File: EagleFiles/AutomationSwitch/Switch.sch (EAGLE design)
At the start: 28 parts, among them IC1 5V, U1 ATMEGA328P_PDIP

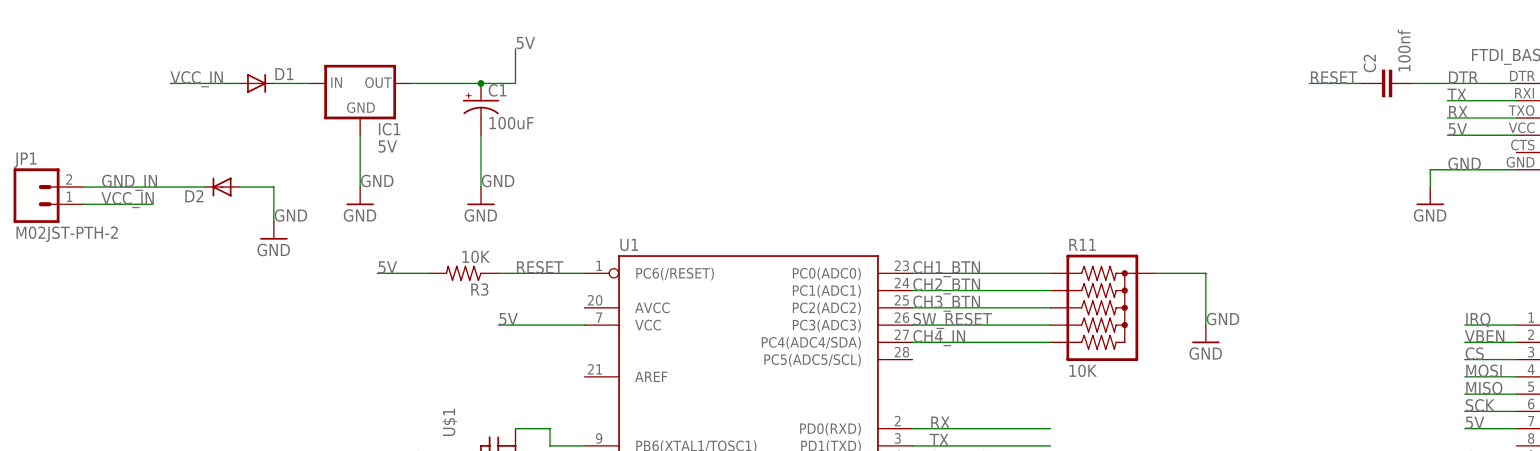
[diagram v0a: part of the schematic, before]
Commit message: Reworked routing and power
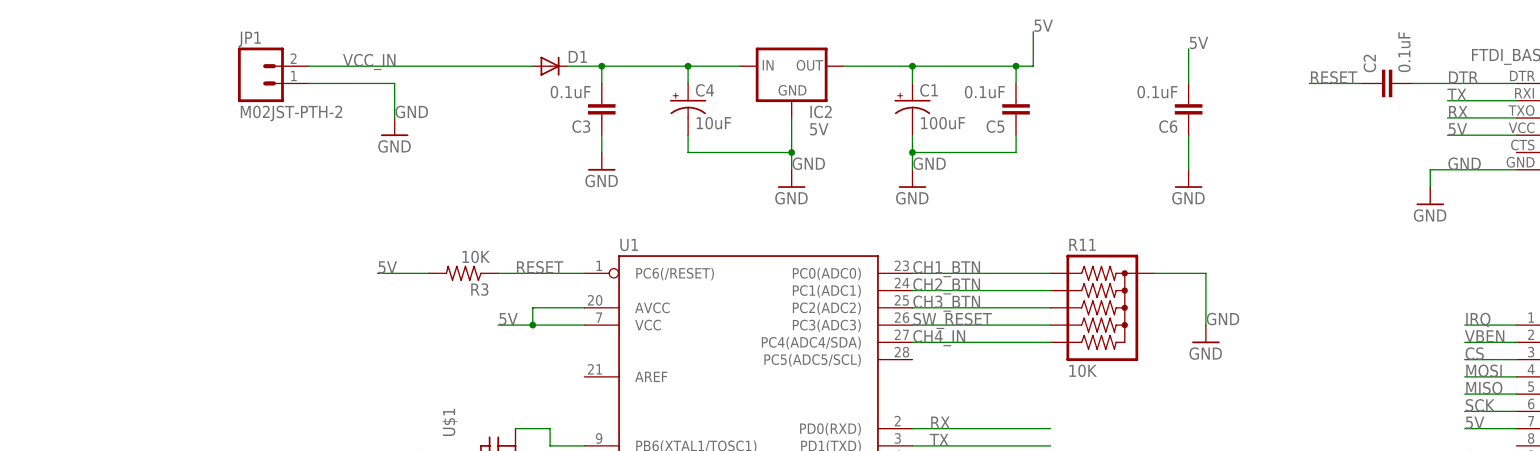
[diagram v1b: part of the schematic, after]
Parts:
- removed D2: (no value), SparkFun-DiscreteSemi:DIODEPTH
- removed IC1: 5V, SparkFun-PowerIC:V_REG_78XXSIDE
- added C3, C5, C6: 0.1uF, SparkFun-Passives:CAPPTH
- added C4: 10uF, SparkFun-Passives:CAP_POLPTH1
- added IC2: 5V, v-reg:78XXS
- C2: value 100nf -> 0.1uF
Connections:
- removed net GND_IN: D2.C, JP1.2
- net 5V: now also C5.2, C6.2, IC2.OUT, U1.AVCC; no longer IC1.OUT
- net GND: now also C3.1, C4.-, C5.1, C6.1, IC2.GND, JP1.1; no longer D2.A, IC1.GND
- net N$10: now also C3.2, C4.+, IC2.IN; no longer IC1.IN
- net VCC_IN: now also JP1.2; no longer JP1.1
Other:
- moved on the sheet: C1, D1, JP1

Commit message: Optimized the Routing
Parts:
- added PULL_DOWN_CH4: SOLDERJUMPERNO, SparkFun-Passives:SOLDERJUMPERNO
- JP3: value (none) -> CH4 Exp
- renumbered U$1 to OSC1
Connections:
- new net N$8: PULL_DOWN_CH4.2, R11.6
- net CH4_IN: now also PULL_DOWN_CH4.1; no longer R11.6
- net CH4_OUT: now also U1.PC5(ADC5/SCL); no longer U1.PB1(OC1A)
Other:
- moved on the sheet: R11
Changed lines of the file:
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@@
 <part name="CH2_BTN" library="SparkFun-Electromechanical" deviceset="SWITCH-MOMENTARY-2" device="12MM"/>
 <part name="CH3_BTN" library="SparkFun-Electromechanical" deviceset="SWITCH-MOMENTARY-2" device="12MM"/>
-<part name="U$1" library="adafruit" deviceset="CERMOSCILL" device="-THM" value="16MHZ"/>
+<part name="OSC1" library="adafruit" deviceset="CERMOSCILL" device="-THM" value="16MHZ"/>
 <part name="C1" library="SparkFun-Passives" deviceset="CAP_POL" device="PTH1" value="100uF"/>
 <part name="C2" library="SparkFun-Passives" deviceset="CAP" device="PTH" value="0.1uF"/>
 <part name="R11" library="SparkFun-Passives" deviceset="RPACK*" device="-BUSSED-SIP-PTH-5" value="10K"/>
 <part name="JP1" library="SparkFun-Connectors" deviceset="M02" device="JST-PTH-2"/>
-<part name="JP3" library="SparkFun-Connectors" deviceset="M04" device="JST-PTH"/>
+<part name="JP3" library="SparkFun-Connectors" deviceset="M04" device="JST-PTH" value="CH4 Exp"/>
 <part name="D1" library="SparkFun-DiscreteSemi" deviceset="DIODE" device="PTH"/>
 <part name="GND1" library="SparkFun-Aesthetics" deviceset="GND" device=""/>
@@
 <part name="GND6" library="SparkFun-Aesthetics" deviceset="GND" device=""/>
 <part name="IC2" library="v-reg" deviceset="78XXS" device="" value="5V"/>
+<part name="PULL_DOWN_CH4" library="SparkFun-Passives" deviceset="SOLDERJUMPER" device="NO"/>
 </parts>
 <sheets>
@@
 <instance part="CH2_BTN" gate="G$1" x="33.02" y="-162.56"/>
 <instance part="CH3_BTN" gate="G$1" x="33.02" y="-172.72"/>
-<instance part="U$1" gate="G$1" x="76.2" y="-68.58" rot="R270"/>
+<instance part="OSC1" gate="G$1" x="76.2" y="-68.58" rot="R270"/>
 <instance part="C1" gate="G$1" x="139.7" y="-15.24"/>
 <instance part="C2" gate="G$1" x="210.82" y="-12.7" rot="R90"/>
-<instance part="R11" gate="G$1" x="160.02" y="-40.64"/>
+<instance part="R11" gate="G$1" x="170.18" y="-40.64"/>
 <instance part="JP1" gate="G$1" x="43.18" y="-12.7"/>
 <instance part="JP3" gate="G$1" x="231.14" y="-93.98" rot="R180"/>
@@
 <instance part="GND8" gate="1" x="218.44" y="-73.66"/>
 <instance part="GND9" gate="1" x="205.74" y="-101.6"/>
-<instance part="GND10" gate="1" x="182.88" y="-50.8"/>
+<instance part="GND10" gate="1" x="190.5" y="-50.8"/>
 <instance part="GND11" gate="1" x="78.74" y="-104.14"/>
 <instance part="GND12" gate="1" x="129.54" y="-154.94"/>
@@
 <instance part="GND6" gate="1" x="180.34" y="-27.94"/>
 <instance part="IC2" gate="1" x="121.92" y="-10.16"/>
+<instance part="PULL_DOWN_CH4" gate="1" x="160.02" y="-50.8"/>
 </instances>
 <busses>
@@
 </segment>
 <segment>
-<pinref part="U$1" gate="G$1" pin="GND"/>
+<pinref part="OSC1" gate="G$1" pin="GND"/>
 <wire x1="73.66" y1="-68.58" x2="66.04" y2="-68.58" width="0.1524" layer="91"/>
 <label x="66.04" y="-68.58" size="1.778" layer="95"/>
@@
 <segment>
 <pinref part="R11" gate="G$1" pin="1"/>
-<wire x1="175.26" y1="-40.64" x2="182.88" y2="-40.64" width="0.1524" layer="91"/>
-<wire x1="182.88" y1="-40.64" x2="182.88" y2="-48.26" width="0.1524" layer="91"/>
+<wire x1="185.42" y1="-40.64" x2="190.5" y2="-40.64" width="0.1524" layer="91"/>
+<wire x1="190.5" y1="-40.64" x2="190.5" y2="-48.26" width="0.1524" layer="91"/>
 <label x="182.88" y="-48.26" size="1.778" layer="95"/>
 <pinref part="GND10" gate="1" pin="GND"/>
@@
 <segment>
 <pinref part="U1" gate="G$1" pin="PC3(ADC3)"/>
-<wire x1="139.7" y1="-48.26" x2="160.02" y2="-48.26" width="0.1524" layer="91"/>
+<wire x1="139.7" y1="-48.26" x2="170.18" y2="-48.26" width="0.1524" layer="91"/>
 <label x="139.7" y="-48.26" size="1.778" layer="95"/>
 <pinref part="R11" gate="G$1" pin="5"/>
@@
 <segment>
 <pinref part="U1" gate="G$1" pin="PC1(ADC1)"/>
-<wire x1="139.7" y1="-43.18" x2="160.02" y2="-43.18" width="0.1524" layer="91"/>
+<wire x1="139.7" y1="-43.18" x2="170.18" y2="-43.18" width="0.1524" layer="91"/>
 <label x="139.7" y="-43.18" size="1.778" layer="95"/>
 <pinref part="R11" gate="G$1" pin="3"/>
@@
 <segment>
 <pinref part="U1" gate="G$1" pin="PC2(ADC2)"/>
-<wire x1="139.7" y1="-45.72" x2="160.02" y2="-45.72" width="0.1524" layer="91"/>
+<wire x1="139.7" y1="-45.72" x2="170.18" y2="-45.72" width="0.1524" layer="91"/>
 <label x="139.7" y="-45.72" size="1.778" layer="95"/>
 <pinref part="R11" gate="G$1" pin="4"/>
@@
 <segment>
 <pinref part="U1" gate="G$1" pin="PC0(ADC0)"/>
-<wire x1="139.7" y1="-40.64" x2="160.02" y2="-40.64" width="0.1524" layer="91"/>
+<wire x1="139.7" y1="-40.64" x2="170.18" y2="-40.64" width="0.1524" layer="91"/>
 <label x="139.7" y="-40.64" size="1.778" layer="95"/>
 <pinref part="R11" gate="G$1" pin="2"/>
@@
 <net name="N$6" class="0">
 <segment>
-<pinref part="U$1" gate="G$1" pin="IN"/>
+<pinref part="OSC1" gate="G$1" pin="IN"/>
 <wire x1="81.28" y1="-63.5" x2="86.36" y2="-63.5" width="0.1524" layer="91"/>
 <wire x1="86.36" y1="-63.5" x2="86.36" y2="-66.04" width="0.1524" layer="91"/>
@@
 <net name="N$7" class="0">
 <segment>
-<pinref part="U$1" gate="G$1" pin="OUT"/>
+<pinref part="OSC1" gate="G$1" pin="OUT"/>
 <wire x1="81.28" y1="-73.66" x2="86.36" y2="-73.66" width="0.1524" layer="91"/>
 <wire x1="86.36" y1="-73.66" x2="86.36" y2="-71.12" width="0.1524" layer="91"/>
@@
 <segment>
 <pinref part="U1" gate="G$1" pin="PC4(ADC4/SDA)"/>
-<pinref part="R11" gate="G$1" pin="6"/>
-<wire x1="139.7" y1="-50.8" x2="160.02" y2="-50.8" width="0.1524" layer="91"/>
+<pinref part="PULL_DOWN_CH4" gate="1" pin="1"/>
+<wire x1="139.7" y1="-50.8" x2="154.94" y2="-50.8" width="0.1524" layer="91"/>
 <label x="139.7" y="-50.8" size="1.778" layer="95"/>
 </segment>
 </net>
 <net name="CH4_OUT" class="0">
-<segment>
-<pinref part="U1" gate="G$1" pin="PB1(OC1A)"/>
-<wire x1="139.7" y1="-88.9" x2="160.02" y2="-88.9" width="0.1524" layer="91"/>
-<label x="142.24" y="-88.9" size="1.778" layer="95"/>
-</segment>
 <segment>
 <pinref part="JP3" gate="G$1" pin="4"/>
@@
 <label x="213.36" y="-99.06" size="1.778" layer="95"/>
 </segment>
-</net>
+<segment>
+<pinref part="U1" gate="G$1" pin="PC5(ADC5/SCL)"/>
+<wire x1="139.7" y1="-53.34" x2="160.02" y2="-53.34" width="0.1524" layer="91"/>
+<label x="139.7" y="-53.34" size="1.778" layer="95"/>
+</segment>
+</net>
+<net name="N$8" class="0">
+<segment>
+<pinref part="PULL_DOWN_CH4" gate="1" pin="2"/>
+<pinref part="R11" gate="G$1" pin="6"/>
+<wire x1="165.1" y1="-50.8" x2="170.18" y2="-50.8" width="0.1524" layer="91"/>
+</segment>
+</net>

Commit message: Label Rework
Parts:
- JP1: LABEL (none) -> DC IN
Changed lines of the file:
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@@
 <part name="C2" library="SparkFun-Passives" deviceset="CAP" device="PTH" value="0.1uF"/>
 <part name="R11" library="SparkFun-Passives" deviceset="RPACK*" device="-BUSSED-SIP-PTH-5" value="10K"/>
-<part name="JP1" library="SparkFun-Connectors" deviceset="M02" device="JST-PTH-2"/>
+<part name="JP1" library="SparkFun-Connectors" deviceset="M02" device="JST-PTH-2">
+<attribute name="LABEL" value="DC IN"/>
+</part>
 <part name="JP3" library="SparkFun-Connectors" deviceset="M04" device="JST-PTH" value="CH4 Exp"/>
 <part name="D1" library="SparkFun-DiscreteSemi" deviceset="DIODE" device="PTH"/>
@@
 <instance part="C2" gate="G$1" x="210.82" y="-12.7" rot="R90"/>
 <instance part="R11" gate="G$1" x="170.18" y="-40.64"/>
-<instance part="JP1" gate="G$1" x="43.18" y="-12.7"/>
+<instance part="JP1" gate="G$1" x="43.18" y="-12.7">
+<attribute name="LABEL" x="43.18" y="-12.7" size="1.778" layer="96"/>
+</instance>
 <instance part="JP3" gate="G$1" x="231.14" y="-93.98" rot="R180"/>
 <instance part="D1" gate="G$1" x="86.36" y="-10.16"/>

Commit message: Final Cleanup
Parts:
- C4: device SparkFun-Passives:CAP_POLPTH1 -> SparkFun-Passives:CAP_POLPTH2
- CH1_LED, CH2_LED, CH3_LED: value (none) -> Blue
- ERROR_LED: value (none) -> Red
- R10, R6, R7, R8, R9: value (none) -> 2k
- STATUS_LED: value (none) -> Green
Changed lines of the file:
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@@
 <part name="SOFTWARE_RESET" library="SparkFun-Electromechanical" deviceset="TAC_SWITCH" device="PTH"/>
 <part name="R3" library="resistor" deviceset="R-US_" device="0207/15" value="10K"/>
-<part name="R6" library="resistor" deviceset="R-US_" device="0207/15"/>
-<part name="R7" library="resistor" deviceset="R-US_" device="0207/15"/>
-<part name="R8" library="resistor" deviceset="R-US_" device="0207/15"/>
-<part name="R9" library="resistor" deviceset="R-US_" device="0207/15"/>
-<part name="R10" library="resistor" deviceset="R-US_" device="0207/15"/>
-<part name="CH1_LED" library="SparkFun-LED" deviceset="LED" device="3MM"/>
-<part name="CH2_LED" library="SparkFun-LED" deviceset="LED" device="3MM"/>
-<part name="CH3_LED" library="SparkFun-LED" deviceset="LED" device="3MM"/>
-<part name="STATUS_LED" library="SparkFun-LED" deviceset="LED" device="3MM"/>
-<part name="ERROR_LED" library="SparkFun-LED" deviceset="LED" device="3MM"/>
+<part name="R6" library="resistor" deviceset="R-US_" device="0207/15" value="2k"/>
+<part name="R7" library="resistor" deviceset="R-US_" device="0207/15" value="2k"/>
+<part name="R8" library="resistor" deviceset="R-US_" device="0207/15" value="2k"/>
+<part name="R9" library="resistor" deviceset="R-US_" device="0207/15" value="2k"/>
+<part name="R10" library="resistor" deviceset="R-US_" device="0207/15" value="2k"/>
+<part name="CH1_LED" library="SparkFun-LED" deviceset="LED" device="3MM" value="Blue"/>
+<part name="CH2_LED" library="SparkFun-LED" deviceset="LED" device="3MM" value="Blue"/>
+<part name="CH3_LED" library="SparkFun-LED" deviceset="LED" device="3MM" value="Blue"/>
+<part name="STATUS_LED" library="SparkFun-LED" deviceset="LED" device="3MM" value="Green"/>
+<part name="ERROR_LED" library="SparkFun-LED" deviceset="LED" device="3MM" value="Red"/>
 <part name="CH1_BTN" library="SparkFun-Electromechanical" deviceset="SWITCH-MOMENTARY-2" device="12MM"/>
 <part name="CH2_BTN" library="SparkFun-Electromechanical" deviceset="SWITCH-MOMENTARY-2" device="12MM"/>
@@
 <part name="GND13" library="SparkFun-Aesthetics" deviceset="GND" device=""/>
 <part name="C3" library="SparkFun-Passives" deviceset="CAP" device="PTH" value="0.1uF"/>
-<part name="C4" library="SparkFun-Passives" deviceset="CAP_POL" device="PTH1" value="10uF"/>
+<part name="C4" library="SparkFun-Passives" deviceset="CAP_POL" device="PTH2" value="10uF"/>
 <part name="GND4" library="SparkFun-Aesthetics" deviceset="GND" device=""/>
 <part name="C5" library="SparkFun-Passives" deviceset="CAP" device="PTH" value="0.1uF"/>
